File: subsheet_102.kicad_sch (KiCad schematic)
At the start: 0 parts

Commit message: place les principaux circuits -- il manque le symbole pour le PIA MC6821
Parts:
- added U? (x6): 16384-WORD_BY_4-BIT_DYNAMIC_RAM_PHY, Package_DIP:DIP-18_W7.62mm_LongPads, symbol tms4416:16384-WORD_BY_4-BIT_DYNAMIC_RAM_PHY
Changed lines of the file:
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@@
 (kicad_sch (version 20211123) (generator eeschema)
-  (paper "A4")
+  (paper "A4" portrait)
+  (title_block
+    (date "2023-05-12")
+    (rev "DRAFT")
+  )
+  (symbol (lib_id "tms4416:16384-WORD_BY_4-BIT_DYNAMIC_RAM_PHY") (at 55.88 60.96 0) (unit 1)
+    (in_bom yes) (on_board yes)
+    (property "Reference" "U?" (id 0) (at 46.99 43.18 0)
+      (effects (font (size 1.27 1.27)) (justify left top))
+    )
+    (property "Value" "16384-WORD_BY_4-BIT_DYNAMIC_RAM_PHY" (id 1) (at 46.99 45.72 0)
+      (effects (font (size 1.27 1.27) bold) (justify left top))
+    )
+    (property "Footprint" "Package_DIP:DIP-18_W7.62mm_LongPads" (id 2) (at 46.99 40.64 0)
+      (effects (font (size 1.27 1.27)) (justify left top) hide)
+    )
+    (property "Datasheet" "https://raw.githubusercontent.com/sporniket/kicad-symbols-generated/main/reference-materials/commons/memory/tms4416.pdf" (id 3) (at 46.99 38.1 0)
+      (effects (font (size 1.27 1.27)) (justify left top) hide)
+    )
+    (pin "1")
+    (pin "10")
+    (pin "11")
+    (pin "12")
+    (pin "13")
+    (pin "14")
+    (pin "15")
+    (pin "16")
+    (pin "17")
+    (pin "18")
+    (pin "2")
+    (pin "3")
+    (pin "4")
+    (pin "5")
+    (pin "6")
+    (pin "7")
+    (pin "8")
+    (pin "9")
+  )
+  (symbol (lib_id "tms4416:16384-WORD_BY_4-BIT_DYNAMIC_RAM_PHY") (at 135.89 137.16 0) (unit 1)
+    (in_bom yes) (on_board yes)
+    (property "Reference" "U?" (id 0) (at 127 119.38 0)
+      (effects (font (size 1.27 1.27)) (justify left top))
+    )
+    (property "Value" "16384-WORD_BY_4-BIT_DYNAMIC_RAM_PHY" (id 1) (at 127 121.92 0)
+      (effects (font (size 1.27 1.27) bold) (justify left top))
+    )
+    (property "Footprint" "Package_DIP:DIP-18_W7.62mm_LongPads" (id 2) (at 127 116.84 0)
+      (effects (font (size 1.27 1.27)) (justify left top) hide)
+    )
+    (property "Datasheet" "https://raw.githubusercontent.com/sporniket/kicad-symbols-generated/main/reference-materials/commons/memory/tms4416.pdf" (id 3) (at 127 114.3 0)
+      (effects (font (size 1.27 1.27)) (justify left top) hide)
+    )
+    (pin "1")
+    (pin "10")
+    (pin "11")
+    (pin "12")
+    (pin "13")
+    (pin "14")
+    (pin "15")
+    (pin "16")
+    (pin "17")
+    (pin "18")
+    (pin "2")
+    (pin "3")
+    (pin "4")
+    (pin "5")
+    (pin "6")
+    (pin "7")
+    (pin "8")
+    (pin "9")
+  )
+  (symbol (lib_id "tms4416:16384-WORD_BY_4-BIT_DYNAMIC_RAM_PHY") (at 55.88 99.06 0) (unit 1)
+    (in_bom yes) (on_board yes)
+    (property "Reference" "U?" (id 0) (at 46.99 81.28 0)
+      (effects (font (size 1.27 1.27)) (justify left top))
+    )
+    (property "Value" "16384-WORD_BY_4-BIT_DYNAMIC_RAM_PHY" (id 1) (at 46.99 83.82 0)
+      (effects (font (size 1.27 1.27) bold) (justify left top))
+    )
+    (property "Footprint" "Package_DIP:DIP-18_W7.62mm_LongPads" (id 2) (at 46.99 78.74 0)
+      (effects (font (size 1.27 1.27)) (justify left top) hide)
+    )
+    (property "Datasheet" "https://raw.githubusercontent.com/sporniket/kicad-symbols-generated/main/reference-materials/commons/memory/tms4416.pdf" (id 3) (at 46.99 76.2 0)
+      (effects (font (size 1.27 1.27)) (justify left top) hide)
+    )
+    (pin "1")
+    (pin "10")
+    (pin "11")
+    (pin "12")
+    (pin "13")
+    (pin "14")
+    (pin "15")
+    (pin "16")
+    (pin "17")
+    (pin "18")
+    (pin "2")
+    (pin "3")
+    (pin "4")
+    (pin "5")
+    (pin "6")
+    (pin "7")
+    (pin "8")
+    (pin "9")
+  )
+  (symbol (lib_id "tms4416:16384-WORD_BY_4-BIT_DYNAMIC_RAM_PHY") (at 138.43 60.96 0) (unit 1)
+    (in_bom yes) (on_board yes)
+    (property "Reference" "U?" (id 0) (at 129.54 43.18 0)
+      (effects (font (size 1.27 1.27)) (justify left top))
+    )
+    (property "Value" "16384-WORD_BY_4-BIT_DYNAMIC_RAM_PHY" (id 1) (at 129.54 45.72 0)
+      (effects (font (size 1.27 1.27) bold) (justify left top))
+    )
+    (property "Footprint" "Package_DIP:DIP-18_W7.62mm_LongPads" (id 2) (at 129.54 40.64 0)
+      (effects (font (size 1.27 1.27)) (justify left top) hide)
+    )
+    (property "Datasheet" "https://raw.githubusercontent.com/sporniket/kicad-symbols-generated/main/reference-materials/commons/memory/tms4416.pdf" (id 3) (at 129.54 38.1 0)
+      (effects (font (size 1.27 1.27)) (justify left top) hide)
+    )
+    (pin "1")
+    (pin "10")
+    (pin "11")
+    (pin "12")
+    (pin "13")
+    (pin "14")
+    (pin "15")
+    (pin "16")
+    (pin "17")
+    (pin "18")
+    (pin "2")
+    (pin "3")
+    (pin "4")
+    (pin "5")
+    (pin "6")
+    (pin "7")
+    (pin "8")
+    (pin "9")
+  )
+  (symbol (lib_id "tms4416:16384-WORD_BY_4-BIT_DYNAMIC_RAM_PHY") (at 55.88 137.16 0) (unit 1)
+    (in_bom yes) (on_board yes)
+    (property "Reference" "U?" (id 0) (at 46.99 119.38 0)
+      (effects (font (size 1.27 1.27)) (justify left top))
+    )
+    (property "Value" "16384-WORD_BY_4-BIT_DYNAMIC_RAM_PHY" (id 1) (at 46.99 121.92 0)
+      (effects (font (size 1.27 1.27) bold) (justify left top))
+    )
+    (property "Footprint" "Package_DIP:DIP-18_W7.62mm_LongPads" (id 2) (at 46.99 116.84 0)
+      (effects (font (size 1.27 1.27)) (justify left top) hide)
+    )
+    (property "Datasheet" "https://raw.githubusercontent.com/sporniket/kicad-symbols-generated/main/reference-materials/commons/memory/tms4416.pdf" (id 3) (at 46.99 114.3 0)
+      (effects (font (size 1.27 1.27)) (justify left top) hide)
+    )
+    (pin "1")
+    (pin "10")
+    (pin "11")
+    (pin "12")
+    (pin "13")
+    (pin "14")
+    (pin "15")
+    (pin "16")
+    (pin "17")
+    (pin "18")
+    (pin "2")
+    (pin "3")
+    (pin "4")
+    (pin "5")
+    (pin "6")
+    (pin "7")
+    (pin "8")
+    (pin "9")
+  )
+  (symbol (lib_id "tms4416:16384-WORD_BY_4-BIT_DYNAMIC_RAM_PHY") (at 137.16 99.06 0) (unit 1)
+    (in_bom yes) (on_board yes)
+    (property "Reference" "U?" (id 0) (at 128.27 81.28 0)
+      (effects (font (size 1.27 1.27)) (justify left top))
+    )
+    (property "Value" "16384-WORD_BY_4-BIT_DYNAMIC_RAM_PHY" (id 1) (at 128.27 83.82 0)
+      (effects (font (size 1.27 1.27) bold) (justify left top))
+    )
+    (property "Footprint" "Package_DIP:DIP-18_W7.62mm_LongPads" (id 2) (at 128.27 78.74 0)
+      (effects (font (size 1.27 1.27)) (justify left top) hide)
+    )
+    (property "Datasheet" "https://raw.githubusercontent.com/sporniket/kicad-symbols-generated/main/reference-materials/commons/memory/tms4416.pdf" (id 3) (at 128.27 76.2 0)
+      (effects (font (size 1.27 1.27)) (justify left top) hide)
+    )
+    (pin "1")
+    (pin "10")
+    (pin "11")
+    (pin "12")
+    (pin "13")
+    (pin "14")
+    (pin "15")
+    (pin "16")
+    (pin "17")
+    (pin "18")
+    (pin "2")
+    (pin "3")
+    (pin "4")
+    (pin "5")
+    (pin "6")
+    (pin "7")
+    (pin "8")
+    (pin "9")
+  )
 )

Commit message: information schéma, commence le gate array I29
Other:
- title: (none) -> Conversion du Thomson MO5 — Unité centrale
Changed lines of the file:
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@@
   (paper "A4" portrait)
   (title_block
+    (title "Conversion du Thomson MO5 — Unité centrale")
     (date "2023-05-12")
     (rev "DRAFT")
+    (comment 1 "http://github.com/sporniket/kicad-conversions--thomson-mo5--v1")
+    (comment 2 "Dépôt d'origine : ")
+    (comment 4 "Reference : POP5001 501994-01")
   )
   (symbol (lib_id "tms4416:16384-WORD_BY_4-BIT_DYNAMIC_RAM_PHY") (at 55.88 60.96 0) (unit 1)

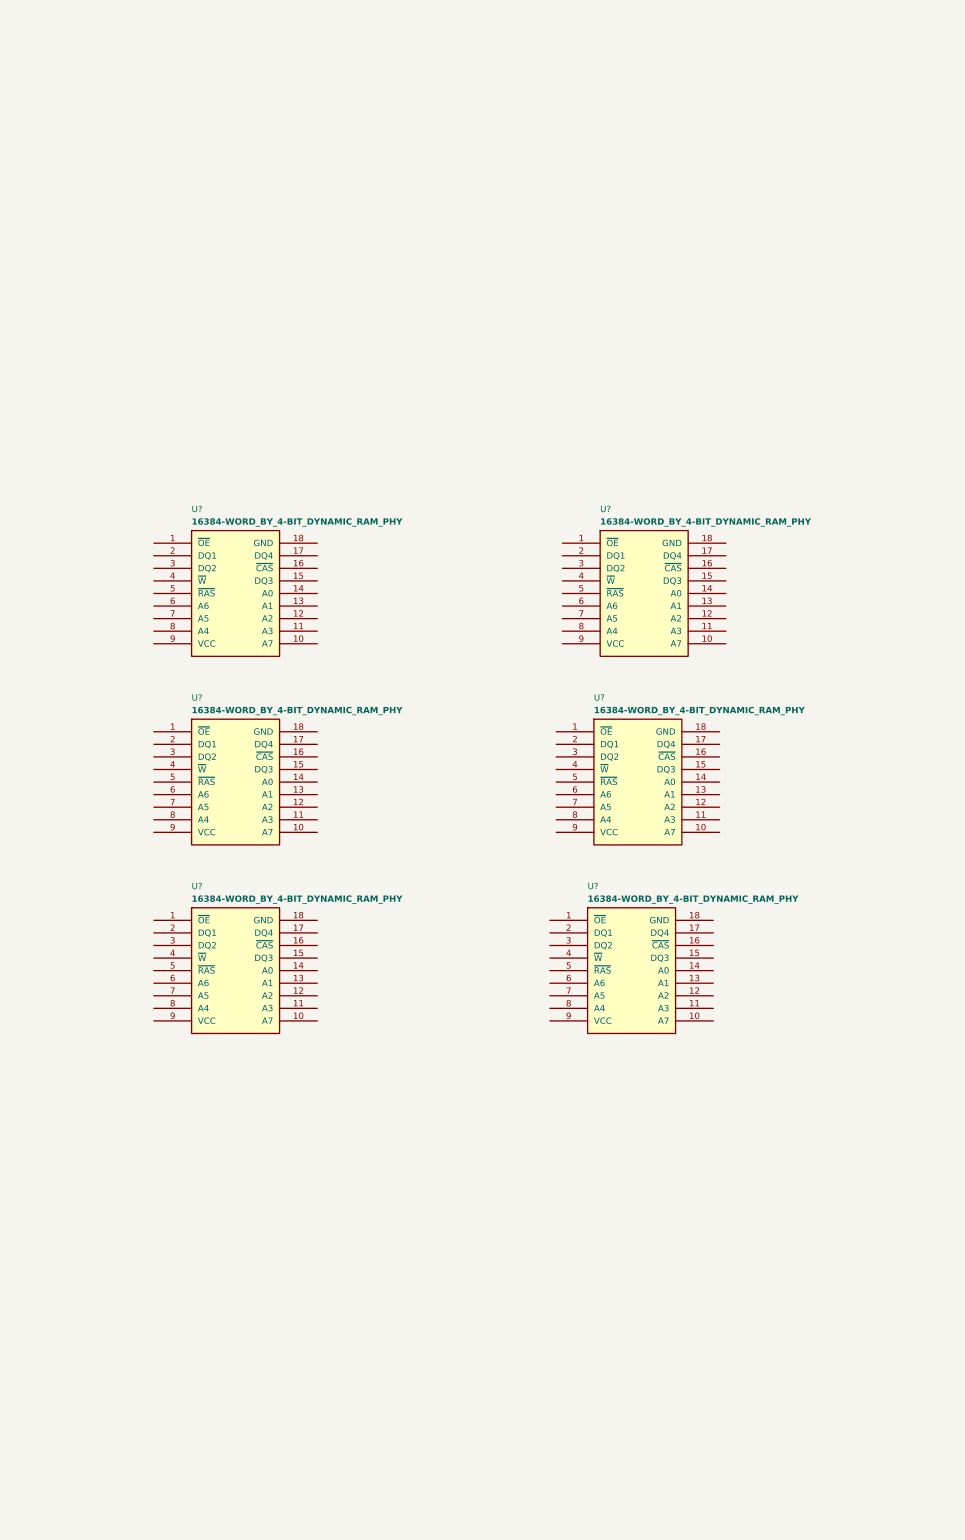
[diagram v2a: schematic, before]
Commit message: RAM : drams, transceiver couleur et point
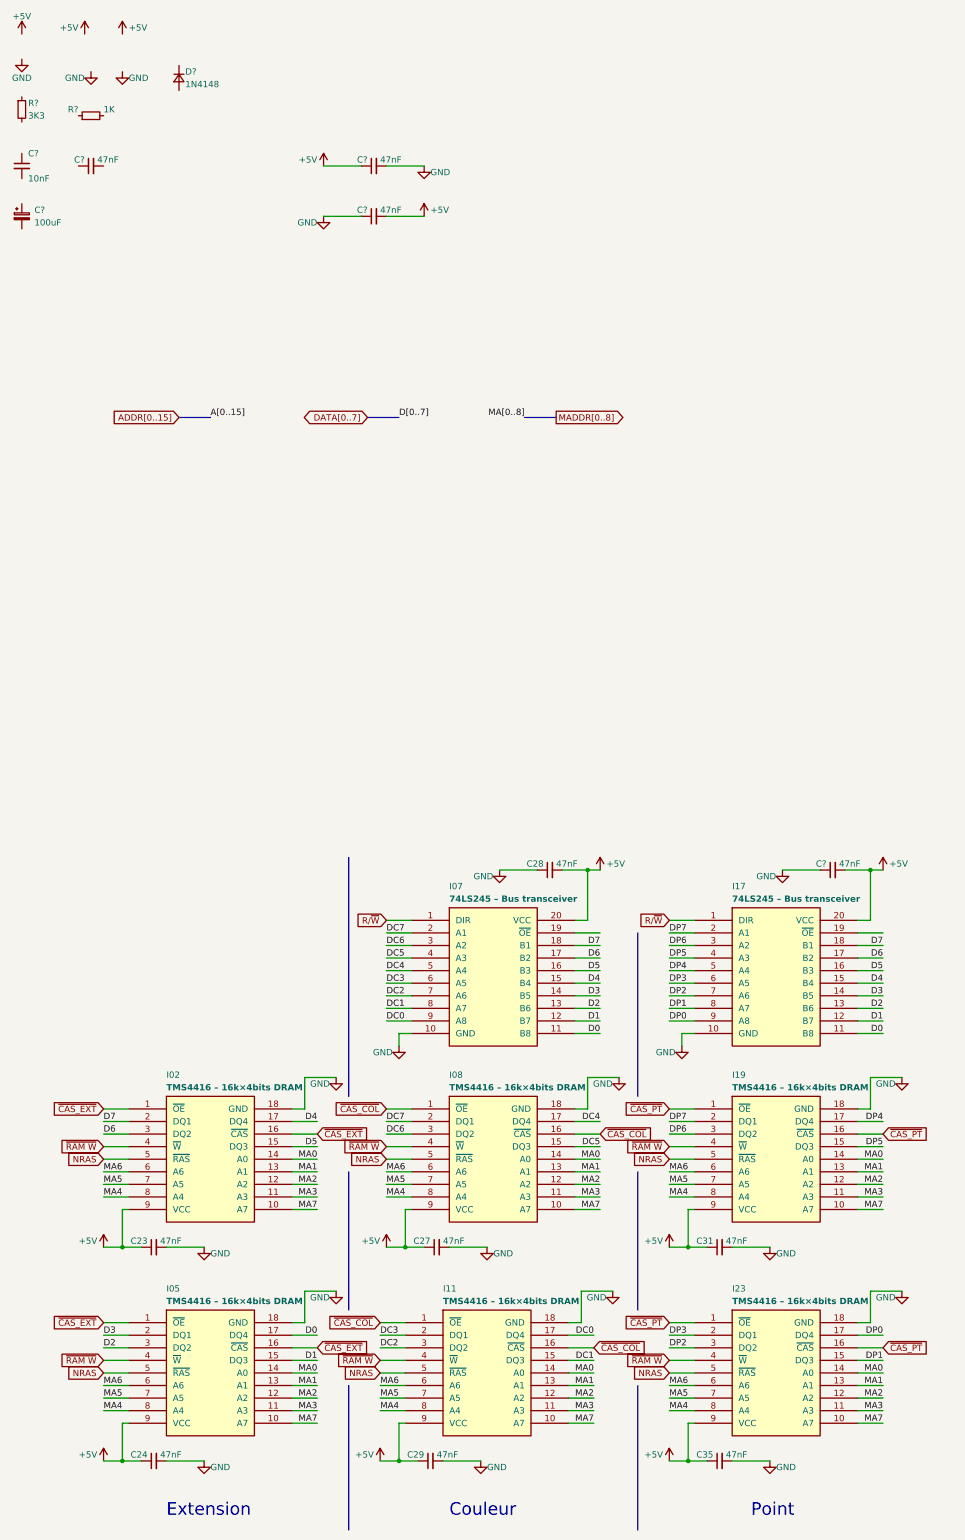
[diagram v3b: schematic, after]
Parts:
- added C23, C24, C27, C28, C29, C31, C35, C? (x4): 47nF, symbol Device:C_Small
- added C?: 100uF, symbol Device:C_Polarized_Small
- added C?: 10nF, symbol Device:C_Small
- added D?: 1N4148, symbol Device:D_Small
- added I07, I17: 74LS245 – Bus transceiver, Package_DIP:DIP-20_W7.62mm_LongPads, symbol 74x245:74X245_OCTAL_BUS_TRANSCEIVERSWITH_3-STATEOUTPUTS_PHY
- added R?: 1K, symbol Device:R_Small
- added R?: 3K3, symbol Device:R_Small
- I02, I05, I08, I11, I19, I23: renamed from U?; value 16384-WORD_BY_4-BIT_DYNAMIC_RAM_PHY -> TMS4416 – 16k×4bits DRAM
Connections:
- net ~{CAS_EXT}: now reaches I02.1 (~{OE})
- net ~{CAS_EXT}: now also I02.16 (~{CAS}), I05.1 (~{OE}), I05.16 (~{CAS})
- net MA7: now reaches I02.10 (A7)
- net MA7: now also I05.10 (A7), I08.10 (A7), I11.10 (A7), I19.10 (A7), I23.10 (A7)
- net MA3: now reaches I02.11 (A3)
- net MA3: now also I05.11 (A3), I08.11 (A3), I11.11 (A3), I19.11 (A3), I23.11 (A3)
- net MA2: now reaches I02.12 (A2)
- net MA2: now also I05.12 (A2), I08.12 (A2), I11.12 (A2), I19.12 (A2), I23.12 (A2)
- net MA1: now reaches I02.13 (A1)
- net MA1: now also I05.13 (A1), I08.13 (A1), I11.13 (A1), I19.13 (A1), I23.13 (A1)
- net MA0: now reaches I02.14 (A0)
- net MA0: now also I05.14 (A0), I08.14 (A0), I11.14 (A0), I19.14 (A0), I23.14 (A0)
- net D5: now reaches I02.15 (DQ3)
- net D5: now also I07.16 (B3), I17.16 (B3)
- net D4: now reaches I02.17 (DQ4)
- net D4: now also I07.15 (B4), I17.15 (B4)
- net GND: now reaches I02.18 (GND)
- net GND: now also I05.18 (GND), I08.18 (GND), I11.18 (GND), I19.18 (GND), I23.18 (GND), C23.2, C24.2, C27.2, C28.1, C29.2, C31.2, C35.2, C?.1, C?.1, C?.2, I07.10 (GND), I17.10 (GND)
- net D7: now reaches I02.2 (DQ1)
- net D7: now also I07.18 (B1), I17.18 (B1)
- net D6: now reaches I02.3 (DQ2)
- net D6: now also I07.17 (B2), I17.17 (B2)
- net ~{RAM W}: now reaches I02.4 (~{W})
- net ~{RAM W}: now also I05.4 (~{W}), I08.4 (~{W}), I11.4 (~{W}), I19.4 (~{W}), I23.4 (~{W})
- net NRAS: now reaches I02.5 (~{RAS})
- net NRAS: now also I05.5 (~{RAS}), I08.5 (~{RAS}), I11.5 (~{RAS}), I19.5 (~{RAS}), I23.5 (~{RAS})
- net MA6: now reaches I02.6 (A6)
- net MA6: now also I05.6 (A6), I08.6 (A6), I11.6 (A6), I19.6 (A6), I23.6 (A6)
- net MA5: now reaches I02.7 (A5)
- net MA5: now also I05.7 (A5), I08.7 (A5), I11.7 (A5), I19.7 (A5), I23.7 (A5)
- net MA4: now reaches I02.8 (A4)
- net MA4: now also I05.8 (A4), I08.8 (A4), I11.8 (A4), I19.8 (A4), I23.8 (A4)
- net +5V: now reaches I02.9 (VCC)
- net +5V: now also I05.9 (VCC), I08.9 (VCC), I11.9 (VCC), I19.9 (VCC), I23.9 (VCC), C23.1, C24.1, C27.1, C28.2, C29.1, C31.1, C35.1, C?.1, C?.2, C?.2, I07.20 (VCC), I17.20 (VCC)
- net ~{CAS_PT}: now reaches I23.1 (~{OE})
- net ~{CAS_PT}: now also I19.1 (~{OE}), I19.16 (~{CAS}), I23.16 (~{CAS})
- net DP1: now reaches I23.15 (DQ3)
- net DP1: now also I17.8 (A7)
- net DP0: now reaches I23.17 (DQ4)
- net DP0: now also I17.9 (A8)
- net DP3: now reaches I23.2 (DQ1)
- net DP3: now also I17.6 (A5)
- net DP2: now reaches I23.3 (DQ2)
- net DP2: now also I17.7 (A6)
- net ~{CAS_COL}: now reaches I08.1 (~{OE})
- net ~{CAS_COL}: now also I08.16 (~{CAS}), I11.1 (~{OE}), I11.16 (~{CAS})
- net DC5: now reaches I08.15 (DQ3)
- net DC5: now also I07.4 (A3)
- net DC4: now reaches I08.17 (DQ4)
- net DC4: now also I07.5 (A4)
- net DC7: now reaches I08.2 (DQ1)
- net DC7: now also I07.2 (A1)
- net DC6: now reaches I08.3 (DQ2)
- net DC6: now also I07.3 (A2)
- net D1: now reaches I05.15 (DQ3)
- net D1: now also I07.12 (B7), I17.12 (B7)
- net D0: now reaches I05.17 (DQ4)
- net D0: now also I07.11 (B8), I17.11 (B8)
- net D3: now reaches I05.2 (DQ1)
- net D3: now also I07.14 (B5), I17.14 (B5)
- net D2: now reaches I05.3 (DQ2)
- net D2: now also I07.13 (B6), I17.13 (B6)
- net DP5: now reaches I19.15 (DQ3)
- net DP5: now also I17.4 (A3)
- net DP4: now reaches I19.17 (DQ4)
- net DP4: now also I17.5 (A4)
- net DP7: now reaches I19.2 (DQ1)
- net DP7: now also I17.2 (A1)
- net DP6: now reaches I19.3 (DQ2)
- net DP6: now also I17.3 (A2)
- net DC1: now reaches I11.15 (DQ3)
- net DC1: now also I07.8 (A7)
- net DC0: now reaches I11.17 (DQ4)
- net DC0: now also I07.9 (A8)
- net DC3: now reaches I11.2 (DQ1)
- net DC3: now also I07.6 (A5)
- net DC2: now reaches I11.3 (DQ2)
- net DC2: now also I07.7 (A6)
- new net R/~{W}: I07.1 (DIR), I17.1 (DIR)
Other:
- note added: "Couleur"
- note added: "Extension"
- note added: "Point"
- moved on the sheet: I02, I05, I08, I11, I19, I23

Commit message: RAM : temporairement fini
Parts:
- added C02, C03: 100pF, symbol Device:C_Small
- added C? (x2): 47nF, symbol Device:C_Small
- added I09: 74LS32 – 4× 2-input OR gates, Package_DIP:DIP-14_W7.62mm_LongPads, symbol 74x32:QUADRUPLE_2-INPUTS_POSITIVE-OR_GATES_PHY
- added I12: 74LS11 – 3×3 inputs AND gates, Package_DIP:DIP-14_W7.62mm_LongPads, symbol 74x11:74X11_TRIPLE_3-INPUT_POSITIVE-AND_GATES_PHY
- added R29, R34: 100, symbol Device:R_Small
- gave numbers to parts that had none: 1
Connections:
- net +5V: now also C?.2, C?.2, I09.14 (VCC), I12.1 (1A), I12.14 (VCC), I12.5 (2C)
- net GND: now also C02.2, C03.2, C?.1, C?.1, I09.7 (GND), I12.7 (GND)
- net R/~{W}: now also I09.10 (3B), I12.2 (1B), I12.4 (2B)
- net ~{CAS_COL}: now also I12.13 (1C)
- net ~{CAS_PT}: now also I12.3 (2A)
- net at I17.19 (~{OE}): now also C03.1, R34.1
- net ColEnable: now reaches I07.19 (~{OE})
- net ColEnable: now also C02.1, R29.1
- net NRAS renamed nRAS
- net nRAS: now also I12.8 (3Y)
- net ~{RAM W} renamed ~{RamW}
- net ~{RamW}: now also I09.8 (3Y)
- new net: I09.1 (1A), I12.12 (1Y)
- new net: I09.4 (2A), I12.6 (2Y)
- new net: I09.3 (1Y), R29.2
- new net: I09.6 (2Y), R34.2
- new net LIGHT PEN 4: I09.13 (3B)
- new net LIGHT PEN INT: I09.11 (4Y)
- new net ~{GA_E}: I09.2 (1B), I09.5 (2B), I09.9 (3A)
- new net ~{RAS}: I12.10 (3B)
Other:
- note added: "de I45-5"
- note added: "de I46-7"
- note added: "de I47-5"
